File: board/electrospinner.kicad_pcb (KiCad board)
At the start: 2 copper layers, 42 parts, among them J1 12Vin, J2 Programmer, J3 MotorConnector, J4 TempSensorConnector, J5 USB_B, SW1 ResetBTN, U1 TPS62147, U2 FT230XS, U3 MSP430G2553IPW20

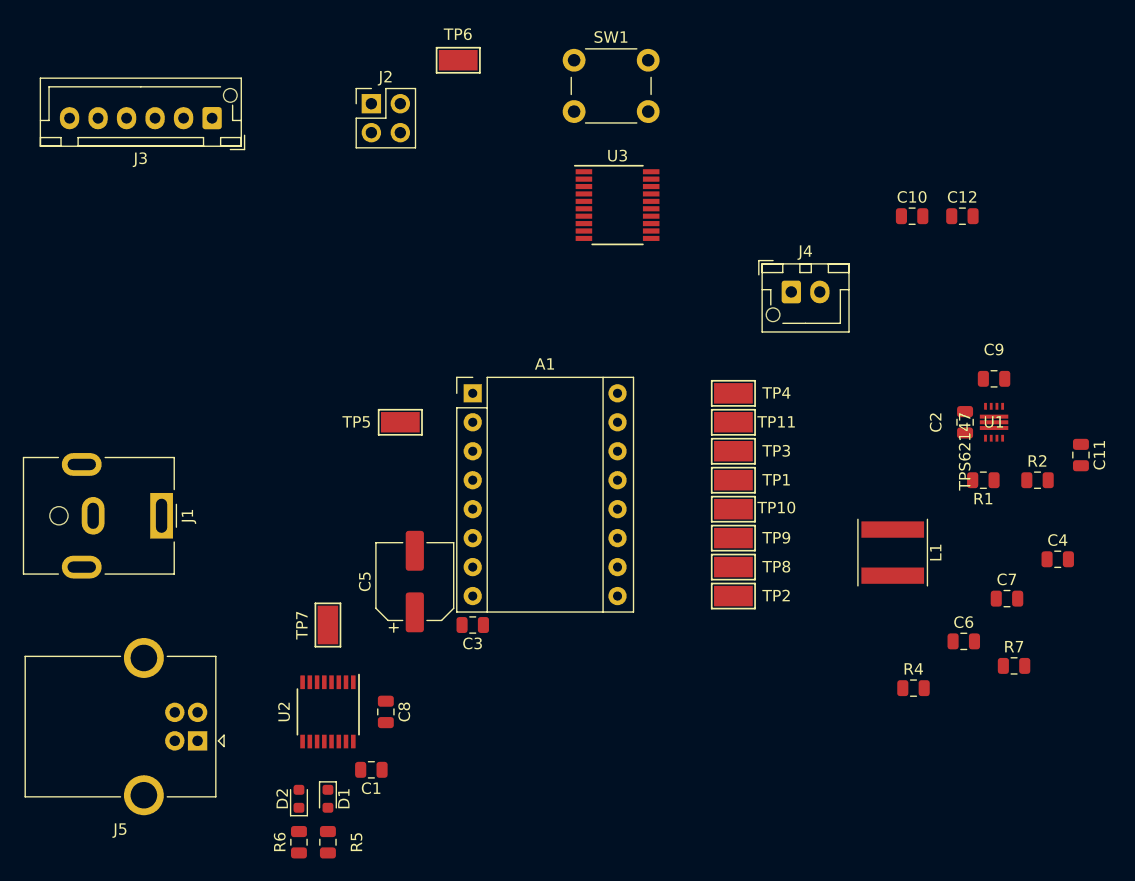
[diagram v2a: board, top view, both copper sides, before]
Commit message: Updates for rev7
Adds project specific symbol and footprint libraries
Adds thermocouple_amplifier datasheet
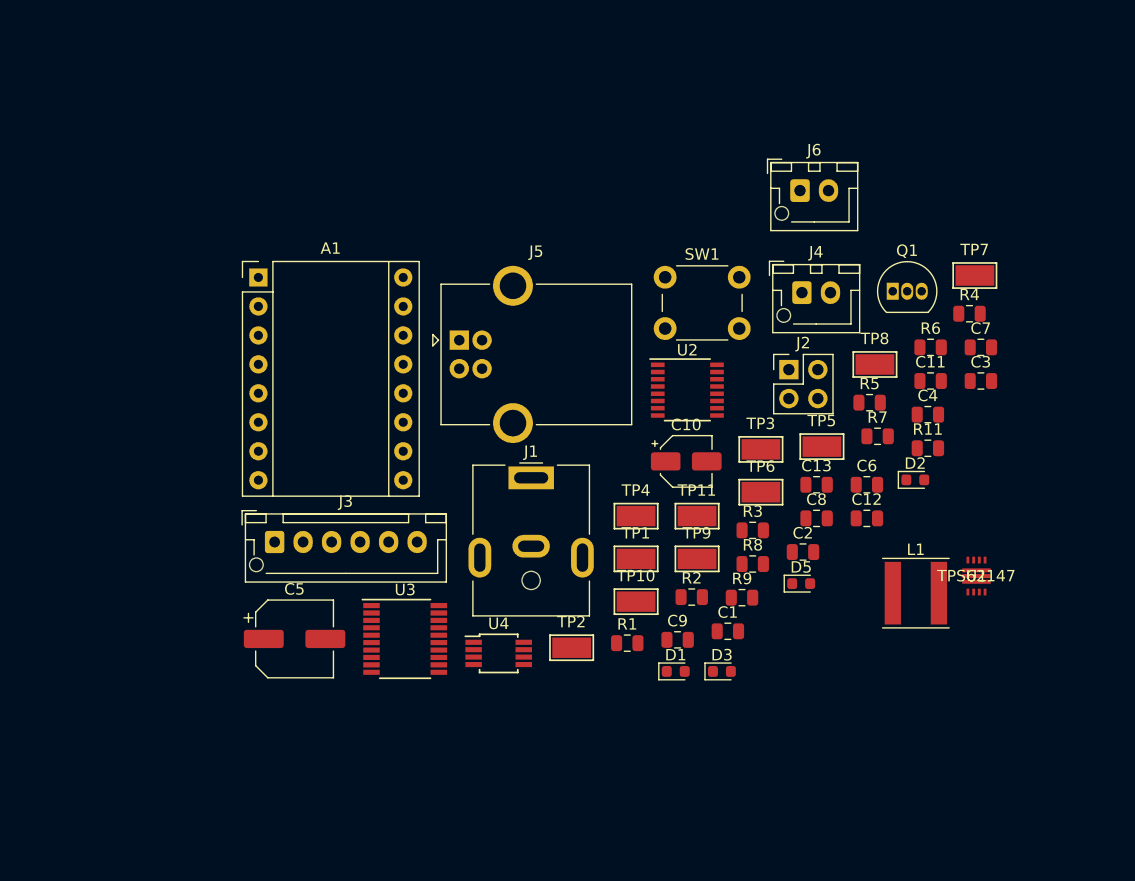
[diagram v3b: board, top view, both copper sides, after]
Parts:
- added C13: 0.1uF, Capacitor_SMD:C_0805_2012Metric, F.Cu at (167.3, 91.8)
- added D3: LedRED, LED_SMD:LED_0603_1608Metric, F.Cu at (159.0, 108.2)
- added D5: LedGRN, LED_SMD:LED_0603_1608Metric, F.Cu at (166.0, 100.5)
- added J6: FanConnector, Connector_JST:JST_XH_B2B-XH-AM_1x02_P2.50mm_Vertical, F.Cu at (165.9, 66.0)
- added Q1: 2N7000, Package_TO_SOT_THT:TO-92_Inline, F.Cu at (174.0, 74.9)
- added R11: 390, Resistor_SMD:R_0805_2012Metric, F.Cu at (177.1, 88.6)
- added R3: 75k, Resistor_SMD:R_0805_2012Metric, F.Cu at (161.7, 95.8)
- added R8: 1M, Resistor_SMD:R_0805_2012Metric, F.Cu at (161.7, 98.8)
- added R9: 390, Resistor_SMD:R_0805_2012Metric, F.Cu at (160.8, 101.7)
- added U4: AD8495, Package_SO:MSOP-8_3x3mm_P0.65mm, F.Cu at (139.4, 106.6)
- C10: value 10uF -> 1uF; footprint Capacitor_SMD:C_0805_2012Metric -> Capacitor_SMD:CP_Elec_4x5.4
- D1: value RXLED -> LedRX
- D2: value TXLED -> LedTX
- L1: footprint electrospinner:L_Coilcraft_XEL6030 -> libs:L_Coilcraft_XEL6030
- R7: value 158 -> 75k
- U1: footprint footprints:TPS62147RGXR -> libs:TPS62147RGXR
- moved R6 70.4 mm to (177.3, 79.8), turned to 0 degrees
- moved TP7 64.5 mm to (181.2, 73.5), turned to 0 degrees
- moved R5 61.2 mm to (172.0, 84.6), turned to 0 degrees
- moved D2 60.9 mm to (176.0, 91.4), turned to 0 degrees
- moved C3 49.4 mm to (181.7, 82.7), turned to 0 degrees
- moved TP6 46.3 mm to (162.4, 92.5)
- moved J2 43.4 mm to (164.9, 81.7)
- moved U3 42.4 mm to (131.2, 105.4)
- moved U2 42.3 mm to (156.0, 83.5), turned to 0 degrees
- moved J5 42.0 mm to (136.0, 79.2), turned to 0 degrees
- moved C8 41.4 mm to (167.3, 94.8), turned to 0 degrees
- moved J3 37.6 mm to (119.8, 96.9), turned to 0 degrees
- moved TP5 37.0 mm to (167.8, 88.5)
- moved C9 36.0 mm to (155.1, 105.4), turned to 0 degrees
- moved R1 34.3 mm to (150.7, 105.7), turned to 0 degrees
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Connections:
- net /~RXLED renamed /~LedRX
- net /~TXLED renamed /~LedTX
- A1 pad 1: GNDD -> GND
- A1 pad 7: GNDD -> GND
- A1 pad 8: +12V -> Net-(A1-Pad8)
- C1 pad 1: +12V -> Net-(C1-Pad1)
- C1 pad 2: GNDD -> GND
- C10 pad 1: +3V3 -> Net-(C10-Pad1)
- C10 pad 2: GNDD -> Net-(C10-Pad2)
- C11 pad 2: GNDD -> GND
- C12 pad 2: GNDD -> GND
- C2 pad 2: GNDD -> GND
- C3 pad 2: GNDD -> Net-(C1-Pad1)
- C4 pad 1: +12V -> +3V3
- C4 pad 2: GNDD -> Net-(C4-Pad2)
- C5 pad 2: GNDD -> Net-(A1-Pad8)
- C6 pad 2: GNDD -> Net-(C6-Pad2)
- C7 pad 2: GNDD -> Net-(C7-Pad2)
- C8 pad 2: GNDD -> Net-(C8-Pad2)
- C9 pad 1: +3V3 -> GND
- C9 pad 2: GNDD -> Net-(C10-Pad1)
- J1 pad 2: GNDD -> GND
- J1 pad MP: GNDD -> GND
- J2 pad 2: GNDD -> GND
- J4 pad 1: +3V3 -> Net-(J4-Pad1)
- J4 pad 2: /Vo,temp -> Net-(J4-Pad2)
- J5 pad 4: GNDD -> GND
- J5 pad 5: GNDD -> GND
- R2 pad 2: GNDD -> GND
- R7 pad 1: /Vo,temp -> Net-(J4-Pad2)
- R7 pad 2: GNDD -> Net-(C10-Pad2)
- SW1 pad 1: GNDD -> GND
- U1 pad 1: +12V -> Net-(C1-Pad1)
- U1 pad 10: GNDD -> GND
- U1 pad 11: GNDD -> GND
- U1 pad 3: GNDD -> GND
- U1 pad 4: GNDD -> GND
- U1 pad 7: GNDD -> GND
- U1 pad 8: +12V -> Net-(C1-Pad1)
- U2 pad 12: +3V3 -> Net-(C7-Pad2)
- U2 pad 13: GNDD -> GND
- U2 pad 3: +3V3 -> Net-(C8-Pad2)
- U2 pad 5: GNDD -> GND
- U3 pad 1: +3V3 -> Net-(C6-Pad2)
- U3 pad 13: (no net) -> /MotorM0
- U3 pad 15: (no net) -> /LedGRN
- U3 pad 18: (no net) -> /MotorM2
- U3 pad 19: (no net) -> /MotorM1
- U3 pad 20: GNDD -> GND
- U3 pad 5: /MotorM0 -> /LedRED
- U3 pad 6: /MotorM1 -> /LedGRN
- U3 pad 7: /MotorM2 -> /FAN
